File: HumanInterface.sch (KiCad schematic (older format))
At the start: 2 parts

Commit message: Done with preliminary schematic. Needs review
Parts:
- added C401, C402, C403, C404, C405, C406, C407, C408, C409, C410, C411, C412, C413, C414, C415: 0.1u, Capacitor_SMD:C_0603_1608Metric, symbol Device:C_Small
- added R401, R402, R403: 4.7k, Resistor_SMD:R_0603_1608Metric, symbol Device:R_Small
- added R404, R405, R406: 4.7k, Resistor_SMD:R_0603_1608Metric, symbol Device:R
- added SW401, SW402, SW403: SW_Push, symbol Switch:SW_Push
- added SW404: RotaryEncoder_Switch, symbol Device:RotaryEncoder_Switch
- added U401, U403: 74HC193, symbol ReflowOven:74HC193
- added U402: TCA9534, symbol Interface_Expansion:TCA9534
- added U404, U408: HEF4013B, symbol ReflowOven:HEF4013B
- added U405: SN74LVC2G08, symbol ReflowOven:SN74LVC2G08
- added U406: 74LVC2G14, symbol ReflowOven:74LVC2G14
- added U407: 74HC86D, symbol ReflowOven:74HC86D
- added X401: OSC_4PIN, symbol ReflowOven:OSC_4PIN
- gave numbers to parts that had none: 2
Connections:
- net +3V3: now also C401.1, C402.1, C403.1, C404.1, C405.2, C406.2, C407.2, C411.1, C412.1, C414.1, C415.1, R404.1, R405.1, SW401.1, SW402.1, SW403.1, SW404.S1, U401.11 (~PL), U401.16 (VCC), U402.16 (VDD), U403.11 (~PL), U403.16 (VCC), U404.14 (VDD), U405.8 (VCC), U406.5 (VCC), U407.14 (VCC), U408.14 (VDD), X401.1 (EN), X401.4 (VCC)
- net GND: now also C401.2, C402.2, C403.2, C404.2, C405.1, C406.1, C407.1, C408.2, C409.2, C410.2, C411.2, C412.2, C413.2, C414.2, C415.2, R401.2, R402.2, R403.2, R406.2, SW404.C, U401.1 (D1), U401.10 (D2), U401.14 (MR), U401.15 (D0), U401.8 (GND), U401.9 (D3), U402.1 (A0), U402.2 (A1), U402.3 (A2), U402.8 (GND), U403.1 (D1), U403.10 (D2), U403.14 (MR), U403.15 (D0), U403.8 (GND), U403.9 (D3), U404.7 (VSS), U405.4 (GND), U406.2 (GND), U407.7 (GND), U408.7 (VSS), X401.2 (GND)
- new net: U401.12 (~TCU), U403.5 (CPU)
- new net: U401.13 (~TCD), U403.4 (CPD)
- new net: U405.1 (1A), U407.6 (2Y)
- new net: U407.12 (4A), U407.8 (3Y)
- new net: U405.2 (1B), U405.6 (2B), U407.11 (4Y)
- new net: U407.13 (4B), U407.3 (1Y)
- new net: U405.7 (1Y), U406.6 (1Y), U408.5 (1D)
- new net: U405.3 (2Y), U408.9 (2D)
- new net: U405.5 (2A), U406.1 (1A)
- new net CHANA: R405.2, SW404.A, U404.5 (1D), U407.4 (2A), U407.9 (3A)
- new net CHANB: R404.2, SW404.B, U404.9 (2D), U407.10 (3B)
- new net CNT0: U401.3 (Q0), U402.4 (P0)
- new net CNT1: U401.2 (Q1), U402.5 (P1)
- new net CNT2: U401.6 (Q2), U402.6 (P2)
- new net CNT3: U401.7 (Q3), U402.7 (P3)
- new net CNT4: U402.9 (P4), U403.3 (Q0)
- new net CNT5: U402.10 (P5), U403.2 (Q1)
- new net CNT6: U402.11 (P6), U403.6 (Q2)
- new net CNT7: U402.12 (P7), U403.7 (Q3)
- new net CNT_DN: U401.4 (CPD), U408.13 (2Q)
- new net CNT_UP: U401.5 (CPU), U408.1 (1Q)
- new net I2C_SCL: U402.14 (SCL)
- new net I2C_SDA: U402.15 (SDA)
- new net LGC_CLK: U404.11 (2CP), U404.3 (1CP), U408.11 (2CP), U408.3 (1CP), X401.3 (OUT)
- new net PSA: U404.1 (1Q), U407.1 (1A), U407.5 (2B)
- new net PSB: U404.13 (2Q), U407.2 (1B)
- new net SW1: C410.1, R401.1, SW403.2
- new net SW2: C409.1, R402.1, SW402.2
- new net SW3: C408.1, R403.1, SW401.2
- new net SW_BTN: C413.1, R406.1, SW404.S2
- no-connect marks 2 -> 17
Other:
- note added: "Count Up / Down Logic"
- note added: "Counter"
- note added: "DFF Power"
- note added: "Encoder"
- note added: "I2C Addr = 0b0111000 = 0x38"
- note added: "IO Expander"
- note added: "Logic Chip Power Connections"
- note added: "Spare Buttons"
- note added: "State Flip Flops"

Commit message: Added stuff
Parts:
- FB401: footprint (none) -> Inductor_SMD:L_0603_1608Metric
- U401, U403: footprint (none) -> Package_SO:SOIC-16_3.9x9.9mm_P1.27mm
- U402: footprint (none) -> Package_SO:TSSOP-16_4.4x5mm_P0.65mm
- U404, U407, U408: footprint (none) -> Package_SO:SOIC-14_3.9x8.7mm_P1.27mm
- U405: footprint (none) -> Package_SO:VSSOP-8_2.3x2mm_P0.5mm
- U406: footprint (none) -> Package_SO:TSOP-6_1.65x3.05mm_P0.95mm

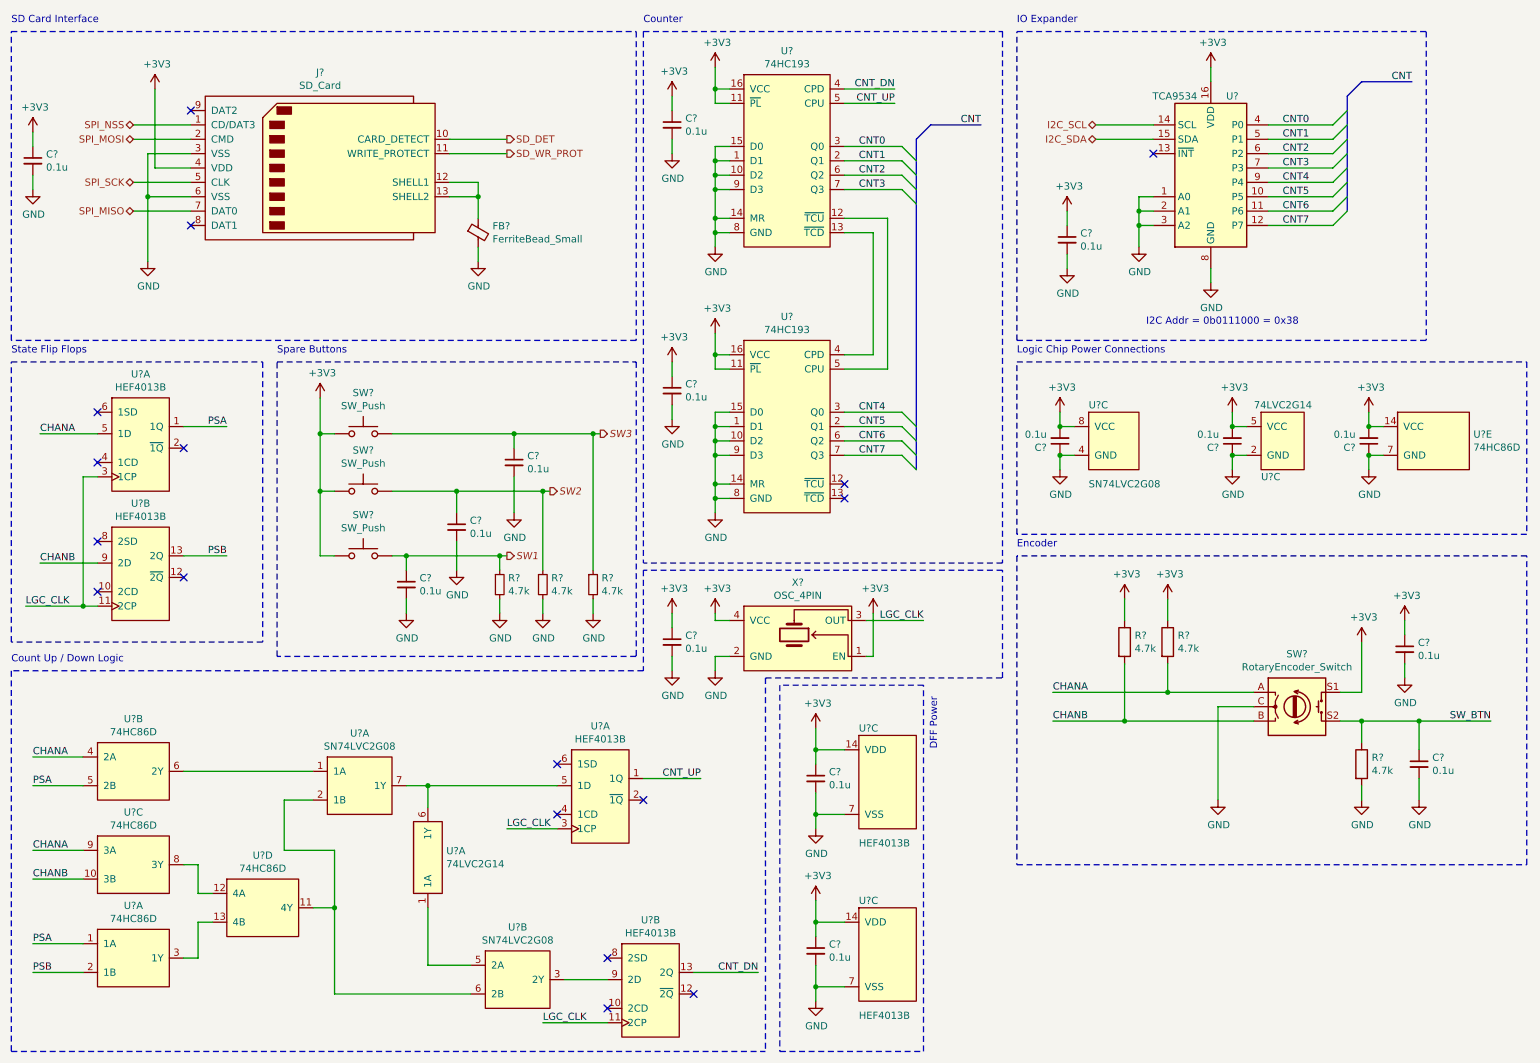
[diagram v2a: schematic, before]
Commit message: Added some footprints
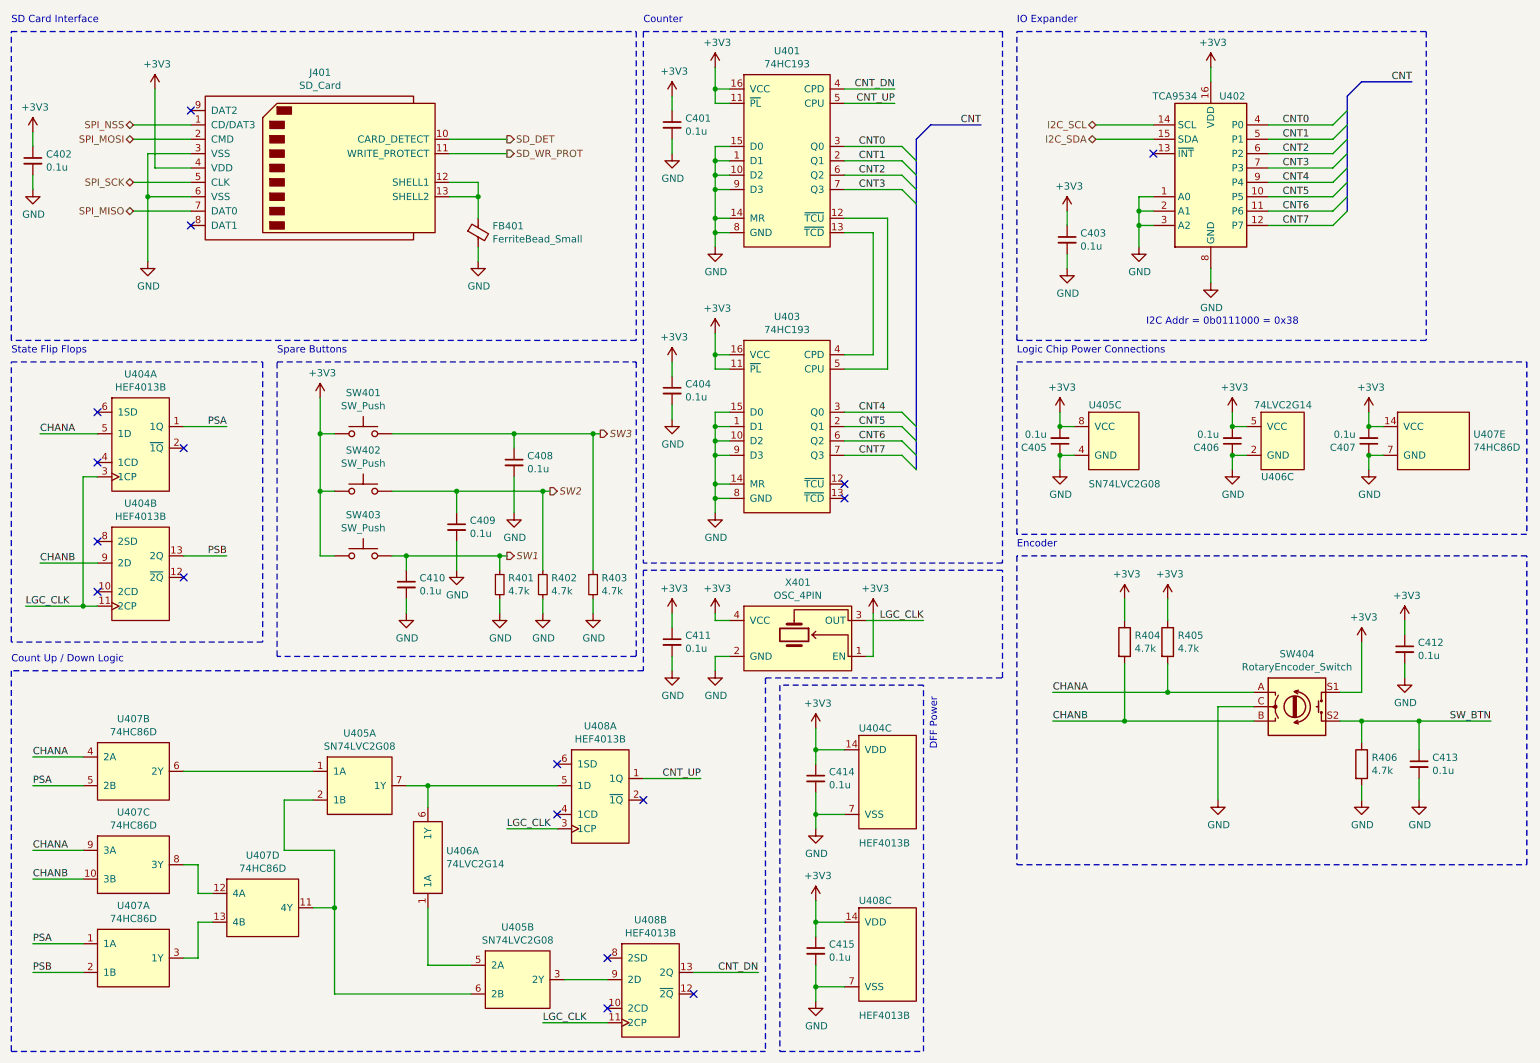
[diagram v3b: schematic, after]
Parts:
- J401: footprint (none) -> ReflowOven:AMPHENOL-10067847

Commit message: Done with footprints
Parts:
- SW401, SW402, SW403: footprint (none) -> ReflowOven:SW_KS11R21CQD
- SW404: footprint (none) -> ReflowOven:EN12-HS22AF20
- X401: footprint (none) -> ReflowOven:KC2016Z48.0000C15XXK
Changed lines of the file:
@@
 F 0 "SW404" H 9500 5717 50  0000 C CNN
 F 1 "RotaryEncoder_Switch" H 9500 5626 50  0000 C CNN
-F 2 "" H 9350 5510 50  0001 C CNN
+F 2 "ReflowOven:EN12-HS22AF20" H 9350 5510 50  0001 C CNN
 F 3 "~" H 9500 5610 50  0001 C CNN
 	1    9500 5350
@@
 F 0 "SW401" H 3000 3735 50  0000 C CNN
 F 1 "SW_Push" H 3000 3644 50  0000 C CNN
-F 2 "" H 3000 3650 50  0001 C CNN
+F 2 "ReflowOven:SW_KS11R21CQD" H 3000 3650 50  0001 C CNN
 F 3 "~" H 3000 3650 50  0001 C CNN
 	1    3000 3450
@@
 F 0 "SW402" H 3000 4135 50  0000 C CNN
 F 1 "SW_Push" H 3000 4044 50  0000 C CNN
-F 2 "" H 3000 4050 50  0001 C CNN
+F 2 "ReflowOven:SW_KS11R21CQD" H 3000 4050 50  0001 C CNN
 F 3 "~" H 3000 4050 50  0001 C CNN
 	1    3000 3850
@@
 F 0 "SW403" H 3000 4585 50  0000 C CNN
 F 1 "SW_Push" H 3000 4494 50  0000 C CNN
-F 2 "" H 3000 4500 50  0001 C CNN
+F 2 "ReflowOven:SW_KS11R21CQD" H 3000 4500 50  0001 C CNN
 F 3 "~" H 3000 4500 50  0001 C CNN
 	1    3000 4300
@@
 F 0 "X401" H 6025 5215 50  0000 C CNN
 F 1 "OSC_4PIN" H 6025 5124 50  0000 C CNN
-F 2 "" V 6000 4850 50  0001 C CNN
+F 2 "ReflowOven:KC2016Z48.0000C15XXK" V 6000 4850 50  0001 C CNN
 F 3 "" V 6000 4850 50  0001 C CNN
 	1    6050 4850

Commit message: Began routing
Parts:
- removed FB401: FerriteBead_Small, Inductor_SMD:L_0603_1608Metric, symbol Device:FerriteBead_Small
- removed J401: SD_Card, ReflowOven:AMPHENOL-10067847, symbol Connector:SD_Card
- added U409: SD-Card-NOSHELL, ReflowOven:AMPHENOL-10067847, symbol ReflowOven:SD-Card-NOSHELL
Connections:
- net +3V3: now also U409.4 (VDD)
- net GND: now also U409.3 (VSS), U409.6 (VSS)
- net SD_DET: now also U409.10 (CARD_DETECT)
- net SD_WR_PROT: now also U409.11 (WRITE_PROTECT)
- net SPI_MISO: now also U409.7 (DAT0)
- net SPI_MOSI: now also U409.2 (CMD)
- net SPI_NSS: now also U409.1 (CD/DAT3)
- net SPI_SCK: now also U409.5 (CLK)
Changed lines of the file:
@@
 Comment4 ""
 $EndDescr
-$Comp
-L Connector:SD_Card J401
-U 1 1 5F6D3AE5
-P 2700 1600
-F 0 "J401" H 2700 2265 50  0000 C CNN
-F 1 "SD_Card" H 2700 2174 50  0000 C CNN
-F 2 "ReflowOven:AMPHENOL-10067847" H 2700 1600 50  0001 C CNN
-F 3 "http://portal.fciconnect.com/Comergent//fci/drawing/10067847.pdf" H 2700 1600 50  0001 C CNN
-	1    2700 1600
-	1    0    0    -1
-$EndComp
 Wire Wire Line
 	1800 1800 1500 1800
@@
 SPI_NSS
 Wire Wire Line
-	3600 1700 3800 1700
-Wire Wire Line
-	3800 1700 3800 1800
-Wire Wire Line
-	3800 1800 3600 1800
-Connection ~ 3800 1800
-$Comp
-L Device:FerriteBead_Small FB401
-U 1 1 5F6D8C36
-P 3800 2050
-F 0 "FB401" H 3900 2096 50  0000 L CNN
-F 1 "FerriteBead_Small" H 3900 2005 50  0000 L CNN
-F 2 "Inductor_SMD:L_0603_1608Metric" V 3730 2050 50  0001 C CNN
-F 3 "~" H 3800 2050 50  0001 C CNN
-	1    3800 2050
-	1    0    0    -1
-$EndComp
-Wire Wire Line
-	3800 1800 3800 1950
-Wire Wire Line
-	3800 2250 3800 2150
-$Comp
-L power:GND #PWR0103
-U 1 1 5F6D832A
-P 3800 2250
-F 0 "#PWR0103" H 3800 2000 50  0001 C CNN
-F 1 "GND" H 3805 2077 50  0000 C CNN
-F 2 "" H 3800 2250 50  0001 C CNN
-F 3 "" H 3800 2250 50  0001 C CNN
-	1    3800 2250
-	1    0    0    -1
-$EndComp
-Wire Wire Line
 	3600 1500 4000 1500
 Text HLabel 4000 1500 2    50   Output ~ 0
@@
 Wire Wire Line
 	700  1450 700  1350
-Text Label 10850 5450 2    50   ~ 0
-SW_BTN
 Wire Notes Line
 	7550 6450 11100 6450
@@
 U 1 1 5F96114C
 P 5950 1300
+AR Path="/5F96114C" Ref="U401"  Part="1"
+AR Path="/5F641779/5F96114C" Ref="U401"  Part="1"
 F 0 "U401" H 5950 1815 50  0000 C CNN
 F 1 "74HC193" H 5950 1724 50  0000 C CNN
@@
 U 1 1 5F962338
 P 5950 3150
+AR Path="/5F962338" Ref="U403"  Part="1"
+AR Path="/5F641779/5F962338" Ref="U403"  Part="1"
 F 0 "U403" H 5950 3665 50  0000 C CNN
 F 1 "74HC193" H 5950 3574 50  0000 C CNN
@@
 	10250 4850 10250 4750
 Wire Wire Line
-	10350 5450 10850 5450
+	10350 5450 10600 5450
 $Comp
 L power:GND #PWR0108
@@
 	1    0    0    -1
 $EndComp
+$Comp
+L ReflowOven:SD-Card-NOSHELL U409
+U 1 1 5F75188E
+P 2700 1550
+F 0 "U409" H 2700 2165 50  0000 C CNN
+F 1 "SD-Card-NOSHELL" H 2700 2074 50  0000 C CNN
+F 2 "ReflowOven:AMPHENOL-10067847" H 2600 2350 50  0001 C CNN
+F 3 "" H 2600 2350 50  0001 C CNN
+	1    2700 1550
+	1    0    0    -1
+$EndComp
 Wire Bus Line
 	9850 1100 9850 1900
 Wire Bus Line
 	6850 1400 6850 3700
+Text HLabel 10600 5450 2    50   Input ~ 0
+SW_BTN
 $EndSCHEMATC
